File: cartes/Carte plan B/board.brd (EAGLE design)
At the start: 49.9 x 73 mm, 20 parts

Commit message: new version + gerber test
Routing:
- added copper zone on layer 1, net GND
- removed copper zone on layer 1, net N$6
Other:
- board text added: "ALIM 12V"
- board text added: "AX12"
- board text added: "BUS CAN"
- board text added: "COMMAND"
- board text added: "I2C"
- board text added: "ISOLATEUR GALVANIQUE"
- board text added: "JUMPER CAN"
- board text added: "ODO_D"
- board text added: "ODO_G"
- board text added: "SHARP"
- board text added: "TRANSCEIVER CAN"
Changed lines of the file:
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@@
 <layer number="23" name="tOrigins" color="15" fill="1" visible="yes" active="yes"/>
 <layer number="24" name="bOrigins" color="15" fill="1" visible="yes" active="yes"/>
-<layer number="25" name="tNames" color="7" fill="1" visible="yes" active="yes"/>
-<layer number="26" name="bNames" color="7" fill="1" visible="yes" active="yes"/>
+<layer number="25" name="tNames" color="7" fill="1" visible="no" active="yes"/>
+<layer number="26" name="bNames" color="7" fill="1" visible="no" active="yes"/>
 <layer number="27" name="tValues" color="7" fill="1" visible="no" active="yes"/>
 <layer number="28" name="bValues" color="7" fill="1" visible="no" active="yes"/>
@@
 <text x="48" y="11" size="1.778" layer="1" rot="R90">Carte_PLAN_B
 ARES_13-14</text>
+<text x="9.27" y="22.98" size="1.778" layer="21" rot="R90">BUS CAN</text>
+<text x="8.6" y="36.67" size="1.4224" layer="21" rot="R90">JUMPER CAN</text>
+<text x="9.17" y="53.71" size="1.4224" layer="21" rot="R90">I2C</text>
+<text x="14.33" y="64.62" size="1.4224" layer="21" rot="R180">SHARP</text>
+<text x="23.69" y="65.77" size="1.4224" layer="21" rot="R180">SHARP</text>
+<text x="32.77" y="65.01" size="1.4224" layer="21" rot="R180">SHARP</text>
+<text x="42.13" y="65.01" size="1.4224" layer="21" rot="R180">SHARP</text>
+<text x="42.52" y="40.21" size="1.4224" layer="21" rot="R270">ODO_G</text>
+<text x="42.8" y="54.76" size="1.4224" layer="21" rot="R270">ODO_D</text>
+<text x="28.85" y="9.38" size="1.4224" layer="21">COMMAND</text>
+<text x="8.6" y="7.95" size="1.4224" layer="21">AX12</text>
+<text x="18.92" y="7.56" size="1.4224" layer="21">AX12</text>
+<text x="2.29" y="19.43" size="1.4224" layer="21">ALIM 12V</text>
+<text x="28.15" y="50.68" size="1.4224" layer="22" rot="MR270">TRANSCEIVER CAN</text>
+<text x="37.37" y="36.18" size="1.4224" layer="22" rot="MR270">ISOLATEUR GALVANIQUE</text>
 </plain>
 <attributes>
@@
 </polygon>
 <via x="25" y="61" extent="1-16" drill="0.4"/>
-<via x="21" y="14" extent="1-16" drill="0.4"/>
 <via x="17" y="8" extent="1-16" drill="0.4"/>
 <via x="37" y="42" extent="1-16" drill="0.4"/>
 <via x="33.48" y="22.97" extent="1-16" drill="0.4"/>
-<via x="30.02" y="23.31" extent="1-16" drill="0.4"/>
-<wire x1="31.59" y1="40.15" x2="37" y2="42" width="0" layer="19" extent="16-16"/>
-<wire x1="25" y1="61" x2="16.94" y2="60.77" width="0" layer="19" extent="1-1"/>
-<wire x1="33.48" y1="22.97" x2="35.195" y2="31.2538" width="0" layer="19" extent="16-16"/>
-<wire x1="30.02" y1="23.31" x2="33.48" y2="22.97" width="0" layer="19" extent="1-1"/>
-<wire x1="21" y1="14" x2="30.02" y2="23.31" width="0" layer="19" extent="1-1"/>
-<wire x1="17" y1="8" x2="21" y2="14" width="0" layer="19" extent="1-1"/>
+<via x="20.93" y="14.05" extent="1-16" drill="0.4"/>
+<via x="29.96" y="23.31" extent="1-16" drill="0.4"/>
+<polygon width="0.254" layer="1">
+<vertex x="0" y="73"/>
+<vertex x="50" y="73"/>
+<vertex x="50" y="0"/>
+<vertex x="0" y="0"/>
+</polygon>
+<via x="23.81" y="39.16" extent="1-16" drill="0.4"/>
+<via x="29.8" y="35.4" extent="1-16" drill="0.4"/>
+<via x="32.95" y="37.36" extent="1-16" drill="0.4"/>
 </signal>
 <signal name="+5V">
@@
 <via x="3" y="3" extent="1-16" drill="2"/>
 </signal>
-<signal name="N$6">
-<polygon width="0.254" layer="1">
-<vertex x="0" y="73"/>
-<vertex x="50" y="73"/>
-<vertex x="50" y="0"/>
-<vertex x="0" y="0"/>
-</polygon>
-</signal>
 <signal name="N$10">

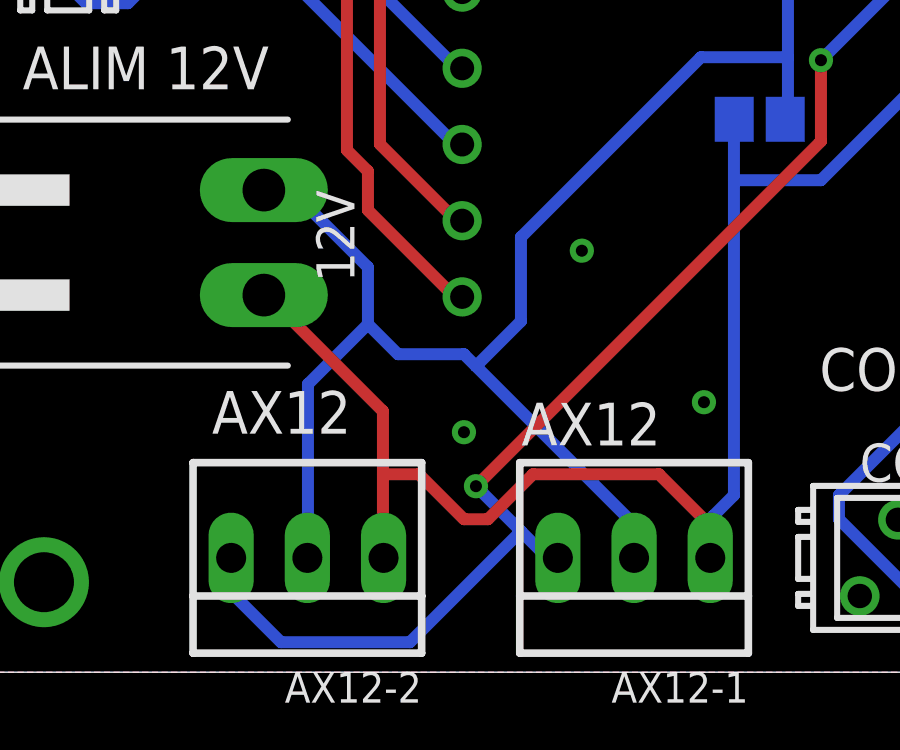
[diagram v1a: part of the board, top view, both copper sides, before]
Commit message: nouvelle version
piste plus large pour le 12V
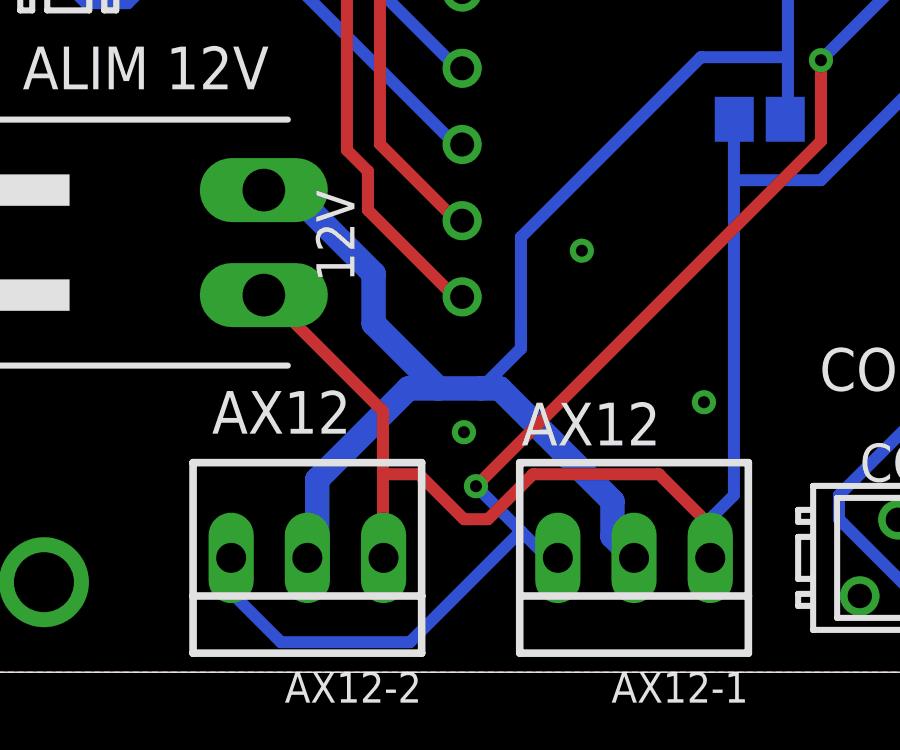
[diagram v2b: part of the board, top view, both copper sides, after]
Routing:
- net +12V_DIRTY: track 53.6 -> 54.9 mm
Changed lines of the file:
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@@
 <wire x1="27.8" y1="18.5" x2="27.71" y2="18.43" width="0.4" layer="16"/>
 <wire x1="31.3" y1="26.3" x2="31.385" y2="26.3262" width="0.4" layer="16"/>
-<wire x1="11.8" y1="9.6" x2="11.8" y2="3.9" width="0.4" layer="16"/>
-<wire x1="13.8" y1="11.6" x2="11.8" y2="9.6" width="0.4" layer="16"/>
-<wire x1="13.8" y1="13.5" x2="13.8" y2="11.6" width="0.4" layer="16"/>
-<wire x1="11.3" y1="16" x2="13.8" y2="13.5" width="0.4" layer="16"/>
-<wire x1="10.4" y1="16" x2="11.3" y2="16" width="0.4" layer="16"/>
 <wire x1="11.8" y1="3.9" x2="11.78" y2="3.81" width="0.4" layer="16"/>
 <wire x1="10.4" y1="16" x2="10.33" y2="16.07" width="0.4" layer="16"/>
 <wire x1="22.6" y1="5" x2="22.6" y2="3.9" width="0.4" layer="16"/>
-<wire x1="17" y1="10.6" x2="17.4" y2="10.2" width="0.4" layer="16"/>
-<wire x1="17.4" y1="10.2" x2="22.6" y2="5" width="0.4" layer="16"/>
-<wire x1="14.8" y1="10.6" x2="17" y2="10.6" width="0.4" layer="16"/>
-<wire x1="13.8" y1="11.6" x2="14.8" y2="10.6" width="0.4" layer="16"/>
 <wire x1="22.6" y1="3.9" x2="22.67" y2="3.81" width="0.4" layer="16"/>
 <wire x1="24.9" y1="20.5" x2="27.8" y2="20.5" width="0.4" layer="16"/>
 <wire x1="18.9" y1="14.5" x2="24.9" y2="20.5" width="0.4" layer="16"/>
 <wire x1="18.9" y1="11.7" x2="18.9" y2="14.5" width="0.4" layer="16"/>
-<wire x1="17.4" y1="10.2" x2="18.9" y2="11.7" width="0.4" layer="16"/>
+<wire x1="10.4" y1="16" x2="11.27" y2="16" width="0.8128" layer="16"/>
+<wire x1="11.27" y1="16" x2="13.99" y2="13.28" width="0.8128" layer="16"/>
+<wire x1="13.99" y1="13.28" x2="13.99" y2="11.62" width="0.8128" layer="16"/>
+<wire x1="13.99" y1="11.62" x2="16.15" y2="9.46" width="0.8128" layer="16"/>
+<wire x1="16.15" y1="9.46" x2="17.57" y2="9.46" width="0.8128" layer="16"/>
+<wire x1="17.57" y1="9.46" x2="18.19" y2="9.46" width="0.8128" layer="16"/>
+<wire x1="18.19" y1="9.46" x2="21.95" y2="5.7" width="0.8128" layer="16"/>
+<wire x1="21.95" y1="5.7" x2="21.95" y2="4.53" width="0.8128" layer="16"/>
+<wire x1="21.95" y1="4.53" x2="22.67" y2="3.81" width="0.8128" layer="16"/>
+<wire x1="16.15" y1="9.46" x2="15.15" y2="9.46" width="0.8128" layer="16"/>
+<wire x1="15.15" y1="9.46" x2="12.11" y2="6.42" width="0.8128" layer="16"/>
+<wire x1="12.11" y1="6.42" x2="12.11" y2="4.14" width="0.8128" layer="16"/>
+<wire x1="12.11" y1="4.14" x2="11.78" y2="3.81" width="0.8128" layer="16"/>
+<wire x1="18.9" y1="11.7" x2="18.9" y2="10.79" width="0.4064" layer="16"/>
+<wire x1="18.9" y1="10.79" x2="17.57" y2="9.46" width="0.4064" layer="16"/>
 </signal>
 <signal name="DATA_AX12">

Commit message: nouvelle version nouveau jumper
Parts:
- removed JUMPERCAN: header-3, jumper:JP2W
- added JUMPER: (no value), pinhead:1X03
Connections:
- net CANH: now also JUMPER.2; no longer JUMPERCAN.2
- net N$9: now also JUMPER.3; no longer JUMPERCAN.1
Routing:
- net +5V: track 209.6 -> 217.6 mm
- net N$9: track 19.8 -> 21.2 mm
- net CANH: track 43.6 -> 45.0 mm
- net DATA_SHARP_1: track 57.7 -> 58.5 mm
- net GND: track 0.00 -> 0.09 mm, vias 9 -> 10

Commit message: plein de trucs
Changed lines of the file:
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@@
 <contactref element="C2" pad="2"/>
 <wire x1="14.24" y1="6.48" x2="14.3" y2="6.6" width="0.4" layer="1"/>
-<wire x1="14.3" y1="6.6" x2="14.3" y2="3.9" width="0.4" layer="1"/>
-<wire x1="10.34" y1="10.38" x2="14.24" y2="6.48" width="0.4" layer="1"/>
+<wire x1="14.3" y1="6.6" x2="14.3" y2="3.9" width="0.8" layer="1"/>
+<wire x1="10.34" y1="10.38" x2="14.24" y2="6.48" width="0.8" layer="1"/>
 <wire x1="14.3" y1="3.9" x2="14.32" y2="3.81" width="0.4" layer="1"/>
-<wire x1="10.34" y1="10.38" x2="10.33" y2="12.57" width="0.4" layer="1"/>
+<wire x1="10.34" y1="10.38" x2="10.33" y2="12.57" width="0.8128" layer="1"/>
 <wire x1="26" y1="5.9" x2="26" y2="16.4" width="0.4" layer="16"/>
 <wire x1="26" y1="16.4" x2="26" y2="18.4" width="0.4" layer="16"/>
@@
 <wire x1="26" y1="16.4" x2="28.9" y2="16.4" width="0.4" layer="16"/>
 <wire x1="35.1" y1="26.3" x2="35.195" y2="26.3262" width="0.4" layer="16"/>
-<wire x1="15.5" y1="6.6" x2="14.3" y2="6.6" width="0.4" layer="1"/>
-<wire x1="17" y1="5.1" x2="15.5" y2="6.6" width="0.4" layer="1"/>
-<wire x1="17.8" y1="5.1" x2="17" y2="5.1" width="0.4" layer="1"/>
-<wire x1="19.3" y1="6.6" x2="17.8" y2="5.1" width="0.4" layer="1"/>
-<wire x1="23.5" y1="6.6" x2="19.3" y2="6.6" width="0.4" layer="1"/>
-<wire x1="25.2" y1="4.9" x2="23.5" y2="6.6" width="0.4" layer="1"/>
+<wire x1="15.5" y1="6.6" x2="14.3" y2="6.6" width="0.8" layer="1"/>
+<wire x1="17" y1="5.1" x2="15.5" y2="6.6" width="0.8" layer="1"/>
+<wire x1="17.8" y1="5.1" x2="17" y2="5.1" width="0.8" layer="1"/>
+<wire x1="19.3" y1="6.6" x2="17.8" y2="5.1" width="0.8" layer="1"/>
+<wire x1="23.5" y1="6.6" x2="19.3" y2="6.6" width="0.8" layer="1"/>
+<wire x1="25.2" y1="4.9" x2="23.5" y2="6.6" width="0.8" layer="1"/>
 <wire x1="25.2" y1="3.9" x2="25.2" y2="4.9" width="0.4" layer="1"/>
 <wire x1="25.2" y1="3.9" x2="25.21" y2="3.81" width="0.4" layer="1"/>

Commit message: nouvelles cartes à jour
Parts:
- added R2: 120, rcl:M0805
- COMMAND: value micromatch-8 -> MMATCH-6-; device con-amp-micromatch:MICROMATCH-8 -> jt-con-micromatch:AMP-215079-6
- moved COMMAND 0.80 mm to (34.3, 3.10)
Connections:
- removed net TF1: COMMAND.8
- removed net TF2: COMMAND.5
- net +12V_DIRTY: now also R2.1
- net DATA_AX12_DIRTY: now also R2.2
- net DIR1: now also COMMAND.3; no longer COMMAND.7
- net DIR2: now also COMMAND.5; no longer COMMAND.4
- net PWM_MOT1: now also COMMAND.4; no longer COMMAND.6
- net PWM_MOT2: now also COMMAND.6; no longer COMMAND.3
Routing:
- net +5V: track 217.6 -> 229.7 mm, vias 3 -> 2
- net PWM_MOT1: track 19.3 -> 10.1 mm
- net +12V_DIRTY: track 54.9 -> 62.3 mm
- net DIR2: track 23.3 -> 16.9 mm
- net DATA_AX12_DIRTY: track 43.8 -> 47.8 mm
- net DIR1: track 11.7 -> 13.2 mm
- net PWM_MOT2: track 16.5 -> 15.2 mm, vias 1 -> 0
